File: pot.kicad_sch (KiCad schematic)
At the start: 7 parts, among them U24 LUM-1502-03_3.5mm_mono_vertic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, U3 LM324

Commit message: almost messed up the opamp :)
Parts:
- renumbered D30 to D1, R78 to R15, R79 to R16, R80 to R17, RV13 to RV1, U3 to U1, U24 to U8
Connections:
- net at RV1.1, U1.1: now also U1.2 (-); no longer U1.3 (+)
- net at R16.2, R17.1: now also U1.3 (+); no longer U1.2 (-)
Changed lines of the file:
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@@
   (symbol (lib_id "eurorack:LUM-1502-03_3.5mm_mono_vertical_jack") (at 33.655 67.31 0) (mirror x)
     (in_bom yes) (on_board yes) (fields_autoplaced)
-    (property "Reference" "U24" (id 0) (at 28.575 65.4049 0)
+    (property "Reference" "U8" (id 0) (at 28.575 65.4049 0)
       (effects (font (size 1.27 1.27)) (justify right))
     )
@@
     (pin "TN")
   )
-  (symbol (lib_id "eurorack:LM324") (at 88.265 63.5 0)
+  (symbol (lib_id "eurorack:LM324") (at 88.265 63.5 0) (mirror x)
     (in_bom yes) (on_board yes) (fields_autoplaced)
-    (property "Reference" "U3" (id 0) (at 88.265 53.34 0))
+    (property "Reference" "U1" (id 0) (at 88.265 53.34 0))
     (property "Value" "LM324" (id 1) (at 88.265 55.88 0))
-    (property "Footprint" "Package_SO:SO-14_3.9x8.65mm_P1.27mm" (id 2) (at 86.995 60.96 0)
+    (property "Footprint" "Package_SO:SO-14_3.9x8.65mm_P1.27mm" (id 2) (at 86.995 66.04 0)
       (effects (font (size 1.27 1.27)) hide)
     )
-    (property "Datasheet" "http://www.ti.com/lit/ds/symlink/lm2902-n.pdf" (id 3) (at 89.535 58.42 0)
+    (property "Datasheet" "http://www.ti.com/lit/ds/symlink/lm2902-n.pdf" (id 3) (at 89.535 68.58 0)
       (effects (font (size 1.27 1.27)) hide)
     )
-    (pin "12")
-    (pin "13")
-    (pin "14")
+    (pin "1")
+    (pin "2")
+    (pin "3")
   )
   (symbol (lib_id "power:GND") (at 39.37 71.12 0) (mirror y)
     (in_bom yes) (on_board yes) (fields_autoplaced)
-    (property "Reference" "#PWR0112" (id 0) (at 39.37 77.47 0)
+    (property "Reference" "#PWR033" (id 0) (at 39.37 77.47 0)
       (effects (font (size 1.27 1.27)) hide)
     )
@@
   (symbol (lib_id "eurorack:BAS 85 VIS") (at 47.625 66.04 180)
     (in_bom yes) (on_board yes) (fields_autoplaced)
-    (property "Reference" "D30" (id 0) (at 47.625 59.055 0))
+    (property "Reference" "D1" (id 0) (at 47.625 59.055 0))
     (property "Value" "BAS 85 VIS" (id 1) (at 47.625 61.595 0))
     (property "Footprint" "Diode_SMD:D_MiniMELF" (id 2) (at 47.625 61.595 0)
@@
   (symbol (lib_id "power:GND") (at 102.87 76.2 0)
     (in_bom yes) (on_board yes) (fields_autoplaced)
-    (property "Reference" "#PWR0114" (id 0) (at 102.87 82.55 0)
+    (property "Reference" "#PWR035" (id 0) (at 102.87 82.55 0)
       (effects (font (size 1.27 1.27)) hide)
     )
@@
   (symbol (lib_id "eurorack:Pot_500") (at 102.87 71.12 0)
     (in_bom yes) (on_board yes) (fields_autoplaced)
-    (property "Reference" "RV13" (id 0) (at 100.965 69.8499 0)
+    (property "Reference" "RV1" (id 0) (at 100.965 69.8499 0)
       (effects (font (size 1.27 1.27)) (justify right))
     )
@@
   (symbol (lib_id "eurorack:R-2k-0805") (at 68.58 69.85 0)
     (in_bom yes) (on_board yes) (fields_autoplaced)
-    (property "Reference" "R80" (id 0) (at 71.12 68.5799 0)
+    (property "Reference" "R17" (id 0) (at 71.12 68.5799 0)
       (effects (font (size 1.27 1.27)) (justify left))
     )
@@
   (symbol (lib_id "eurorack:R-2k-0805") (at 39.37 54.61 0)
     (in_bom yes) (on_board yes) (fields_autoplaced)
-    (property "Reference" "R78" (id 0) (at 41.91 53.3399 0)
+    (property "Reference" "R15" (id 0) (at 41.91 53.3399 0)
       (effects (font (size 1.27 1.27)) (justify left))
     )
@@
   (symbol (lib_id "power:+12V") (at 39.37 49.53 0)
     (in_bom yes) (on_board yes) (fields_autoplaced)
-    (property "Reference" "#PWR0111" (id 0) (at 39.37 53.34 0)
+    (property "Reference" "#PWR032" (id 0) (at 39.37 53.34 0)
       (effects (font (size 1.27 1.27)) hide)
     )
@@
   (symbol (lib_id "power:GND") (at 68.58 75.565 0)
     (in_bom yes) (on_board yes) (fields_autoplaced)
-    (property "Reference" "#PWR0113" (id 0) (at 68.58 81.915 0)
+    (property "Reference" "#PWR034" (id 0) (at 68.58 81.915 0)
       (effects (font (size 1.27 1.27)) hide)
     )
@@
   (symbol (lib_id "eurorack:R-7k5-0805") (at 60.325 66.04 90)
     (in_bom yes) (on_board yes) (fields_autoplaced)
-    (property "Reference" "R79" (id 0) (at 60.325 59.69 90))
+    (property "Reference" "R16" (id 0) (at 60.325 59.69 90))
     (property "Value" "R-7k5-0805" (id 1) (at 60.325 62.23 90))
     (property "Footprint" "Resistor_SMD:R_0805_2012Metric" (id 2) (at 60.325 67.818 90)

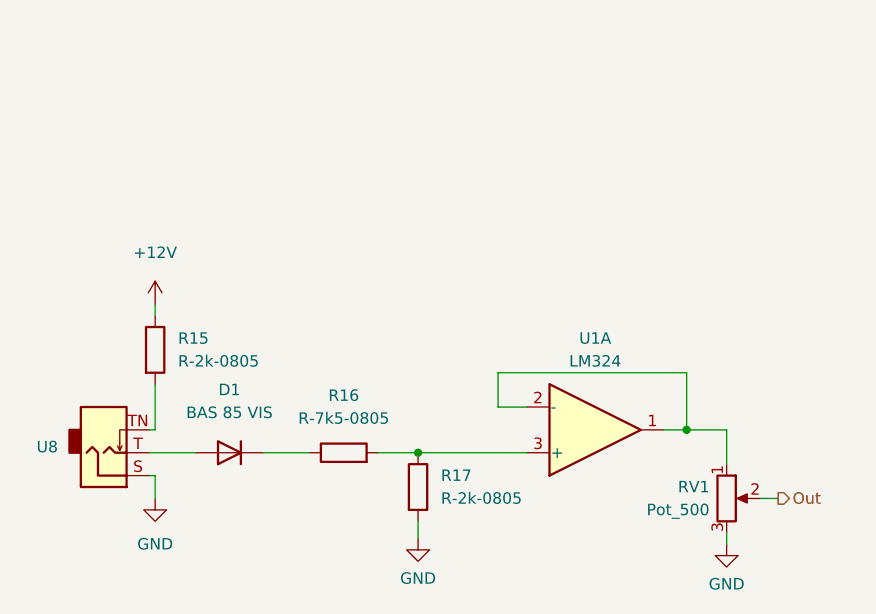
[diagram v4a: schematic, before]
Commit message: Made the first proposed layout
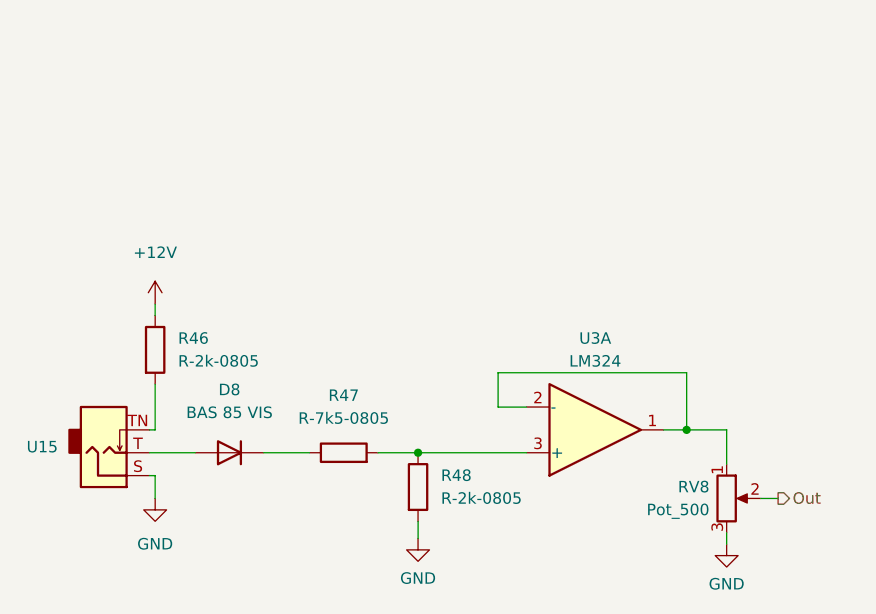
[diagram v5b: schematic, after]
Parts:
- renumbered D1 to D8, R15 to R46, R16 to R47, R17 to R48, RV1 to RV8, U8 to U15, U1 to U3
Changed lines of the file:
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@@
   (symbol (lib_id "eurorack:LUM-1502-03_3.5mm_mono_vertical_jack") (at 33.655 67.31 0) (mirror x)
     (in_bom yes) (on_board yes) (fields_autoplaced)
-    (property "Reference" "U8" (id 0) (at 28.575 65.4049 0)
+    (property "Reference" "U15" (id 0) (at 28.575 65.4049 0)
       (effects (font (size 1.27 1.27)) (justify right))
     )
@@
   (symbol (lib_id "eurorack:LM324") (at 88.265 63.5 0) (mirror x)
     (in_bom yes) (on_board yes) (fields_autoplaced)
-    (property "Reference" "U1" (id 0) (at 88.265 53.34 0))
+    (property "Reference" "U3" (id 0) (at 88.265 53.34 0))
     (property "Value" "LM324" (id 1) (at 88.265 55.88 0))
     (property "Footprint" "Package_SO:SO-14_3.9x8.65mm_P1.27mm" (id 2) (at 86.995 66.04 0)
@@
   (symbol (lib_id "power:GND") (at 39.37 71.12 0) (mirror y)
     (in_bom yes) (on_board yes) (fields_autoplaced)
-    (property "Reference" "#PWR033" (id 0) (at 39.37 77.47 0)
+    (property "Reference" "#PWR071" (id 0) (at 39.37 77.47 0)
       (effects (font (size 1.27 1.27)) hide)
     )
@@
   (symbol (lib_id "eurorack:BAS 85 VIS") (at 47.625 66.04 180)
     (in_bom yes) (on_board yes) (fields_autoplaced)
-    (property "Reference" "D1" (id 0) (at 47.625 59.055 0))
+    (property "Reference" "D8" (id 0) (at 47.625 59.055 0))
     (property "Value" "BAS 85 VIS" (id 1) (at 47.625 61.595 0))
     (property "Footprint" "Diode_SMD:D_MiniMELF" (id 2) (at 47.625 61.595 0)
@@
   (symbol (lib_id "power:GND") (at 102.87 76.2 0)
     (in_bom yes) (on_board yes) (fields_autoplaced)
-    (property "Reference" "#PWR035" (id 0) (at 102.87 82.55 0)
+    (property "Reference" "#PWR073" (id 0) (at 102.87 82.55 0)
       (effects (font (size 1.27 1.27)) hide)
     )
@@
   (symbol (lib_id "eurorack:Pot_500") (at 102.87 71.12 0)
     (in_bom yes) (on_board yes) (fields_autoplaced)
-    (property "Reference" "RV1" (id 0) (at 100.965 69.8499 0)
+    (property "Reference" "RV8" (id 0) (at 100.965 69.8499 0)
       (effects (font (size 1.27 1.27)) (justify right))
     )
@@
   (symbol (lib_id "eurorack:R-2k-0805") (at 68.58 69.85 0)
     (in_bom yes) (on_board yes) (fields_autoplaced)
-    (property "Reference" "R17" (id 0) (at 71.12 68.5799 0)
+    (property "Reference" "R48" (id 0) (at 71.12 68.5799 0)
       (effects (font (size 1.27 1.27)) (justify left))
     )
@@
   (symbol (lib_id "eurorack:R-2k-0805") (at 39.37 54.61 0)
     (in_bom yes) (on_board yes) (fields_autoplaced)
-    (property "Reference" "R15" (id 0) (at 41.91 53.3399 0)
+    (property "Reference" "R46" (id 0) (at 41.91 53.3399 0)
       (effects (font (size 1.27 1.27)) (justify left))
     )
@@
   (symbol (lib_id "power:+12V") (at 39.37 49.53 0)
     (in_bom yes) (on_board yes) (fields_autoplaced)
-    (property "Reference" "#PWR032" (id 0) (at 39.37 53.34 0)
+    (property "Reference" "#PWR070" (id 0) (at 39.37 53.34 0)
       (effects (font (size 1.27 1.27)) hide)
     )
@@
   (symbol (lib_id "power:GND") (at 68.58 75.565 0)
     (in_bom yes) (on_board yes) (fields_autoplaced)
-    (property "Reference" "#PWR034" (id 0) (at 68.58 81.915 0)
+    (property "Reference" "#PWR072" (id 0) (at 68.58 81.915 0)
       (effects (font (size 1.27 1.27)) hide)
     )
@@
   (symbol (lib_id "eurorack:R-7k5-0805") (at 60.325 66.04 90)
     (in_bom yes) (on_board yes) (fields_autoplaced)
-    (property "Reference" "R16" (id 0) (at 60.325 59.69 90))
+    (property "Reference" "R47" (id 0) (at 60.325 59.69 90))
     (property "Value" "R-7k5-0805" (id 1) (at 60.325 62.23 90))
     (property "Footprint" "Resistor_SMD:R_0805_2012Metric" (id 2) (at 60.325 67.818 90)

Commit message: working on the PCB
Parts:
- renumbered D8 to D1, R46 to R15, R47 to R16, R48 to R17, RV8 to RV1, U3 to U1, U15 to U8
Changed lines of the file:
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@@
   (symbol (lib_id "eurorack:LUM-1502-03_3.5mm_mono_vertical_jack") (at 33.655 67.31 0) (mirror x)
     (in_bom yes) (on_board yes) (fields_autoplaced)
-    (property "Reference" "U15" (id 0) (at 28.575 65.4049 0)
+    (property "Reference" "U8" (id 0) (at 28.575 65.4049 0)
       (effects (font (size 1.27 1.27)) (justify right))
     )
@@
   (symbol (lib_id "eurorack:LM324") (at 88.265 63.5 0) (mirror x)
     (in_bom yes) (on_board yes) (fields_autoplaced)
-    (property "Reference" "U3" (id 0) (at 88.265 53.34 0))
+    (property "Reference" "U1" (id 0) (at 88.265 53.34 0))
     (property "Value" "LM324" (id 1) (at 88.265 55.88 0))
     (property "Footprint" "Package_SO:SO-14_3.9x8.65mm_P1.27mm" (id 2) (at 86.995 66.04 0)
@@
   (symbol (lib_id "power:GND") (at 39.37 71.12 0) (mirror y)
     (in_bom yes) (on_board yes) (fields_autoplaced)
-    (property "Reference" "#PWR071" (id 0) (at 39.37 77.47 0)
+    (property "Reference" "#PWR0112" (id 0) (at 39.37 77.47 0)
       (effects (font (size 1.27 1.27)) hide)
     )
@@
   (symbol (lib_id "eurorack:BAS 85 VIS") (at 47.625 66.04 180)
     (in_bom yes) (on_board yes) (fields_autoplaced)
-    (property "Reference" "D8" (id 0) (at 47.625 59.055 0))
+    (property "Reference" "D1" (id 0) (at 47.625 59.055 0))
     (property "Value" "BAS 85 VIS" (id 1) (at 47.625 61.595 0))
     (property "Footprint" "Diode_SMD:D_MiniMELF" (id 2) (at 47.625 61.595 0)
@@
   (symbol (lib_id "power:GND") (at 102.87 76.2 0)
     (in_bom yes) (on_board yes) (fields_autoplaced)
-    (property "Reference" "#PWR073" (id 0) (at 102.87 82.55 0)
+    (property "Reference" "#PWR0114" (id 0) (at 102.87 82.55 0)
       (effects (font (size 1.27 1.27)) hide)
     )
@@
   (symbol (lib_id "eurorack:Pot_500") (at 102.87 71.12 0)
     (in_bom yes) (on_board yes) (fields_autoplaced)
-    (property "Reference" "RV8" (id 0) (at 100.965 69.8499 0)
+    (property "Reference" "RV1" (id 0) (at 100.965 69.8499 0)
       (effects (font (size 1.27 1.27)) (justify right))
     )
@@
   (symbol (lib_id "eurorack:R-2k-0805") (at 68.58 69.85 0)
     (in_bom yes) (on_board yes) (fields_autoplaced)
-    (property "Reference" "R48" (id 0) (at 71.12 68.5799 0)
+    (property "Reference" "R17" (id 0) (at 71.12 68.5799 0)
       (effects (font (size 1.27 1.27)) (justify left))
     )
@@
   (symbol (lib_id "eurorack:R-2k-0805") (at 39.37 54.61 0)
     (in_bom yes) (on_board yes) (fields_autoplaced)
-    (property "Reference" "R46" (id 0) (at 41.91 53.3399 0)
+    (property "Reference" "R15" (id 0) (at 41.91 53.3399 0)
       (effects (font (size 1.27 1.27)) (justify left))
     )
@@
   (symbol (lib_id "power:+12V") (at 39.37 49.53 0)
     (in_bom yes) (on_board yes) (fields_autoplaced)
-    (property "Reference" "#PWR070" (id 0) (at 39.37 53.34 0)
+    (property "Reference" "#PWR0111" (id 0) (at 39.37 53.34 0)
       (effects (font (size 1.27 1.27)) hide)
     )
@@
   (symbol (lib_id "power:GND") (at 68.58 75.565 0)
     (in_bom yes) (on_board yes) (fields_autoplaced)
-    (property "Reference" "#PWR072" (id 0) (at 68.58 81.915 0)
+    (property "Reference" "#PWR0113" (id 0) (at 68.58 81.915 0)
       (effects (font (size 1.27 1.27)) hide)
     )
@@
   (symbol (lib_id "eurorack:R-7k5-0805") (at 60.325 66.04 90)
     (in_bom yes) (on_board yes) (fields_autoplaced)
-    (property "Reference" "R47" (id 0) (at 60.325 59.69 90))
+    (property "Reference" "R16" (id 0) (at 60.325 59.69 90))
     (property "Value" "R-7k5-0805" (id 1) (at 60.325 62.23 90))
     (property "Footprint" "Resistor_SMD:R_0805_2012Metric" (id 2) (at 60.325 67.818 90)

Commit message: working on PCB
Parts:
- renumbered D1 to D28, R15 to R72, R16 to R73, R17 to R74, RV1 to RV11, U8 to U22, U1 to U3
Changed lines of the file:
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@@
   (symbol (lib_id "eurorack:LUM-1502-03_3.5mm_mono_vertical_jack") (at 33.655 67.31 0) (mirror x)
     (in_bom yes) (on_board yes) (fields_autoplaced)
-    (property "Reference" "U8" (id 0) (at 28.575 65.4049 0)
+    (property "Reference" "U22" (id 0) (at 28.575 65.4049 0)
       (effects (font (size 1.27 1.27)) (justify right))
     )
@@
   (symbol (lib_id "eurorack:LM324") (at 88.265 63.5 0) (mirror x)
     (in_bom yes) (on_board yes) (fields_autoplaced)
-    (property "Reference" "U1" (id 0) (at 88.265 53.34 0))
+    (property "Reference" "U3" (id 0) (at 88.265 53.34 0))
     (property "Value" "LM324" (id 1) (at 88.265 55.88 0))
     (property "Footprint" "Package_SO:SO-14_3.9x8.65mm_P1.27mm" (id 2) (at 86.995 66.04 0)
@@
       (effects (font (size 1.27 1.27)) hide)
     )
-    (pin "1")
-    (pin "2")
-    (pin "3")
+    (pin "5")
+    (pin "6")
+    (pin "7")
   )
   (symbol (lib_id "power:GND") (at 39.37 71.12 0) (mirror y)
     (in_bom yes) (on_board yes) (fields_autoplaced)
-    (property "Reference" "#PWR0112" (id 0) (at 39.37 77.47 0)
+    (property "Reference" "#PWR0104" (id 0) (at 39.37 77.47 0)
       (effects (font (size 1.27 1.27)) hide)
     )
@@
   (symbol (lib_id "eurorack:BAS 85 VIS") (at 47.625 66.04 180)
     (in_bom yes) (on_board yes) (fields_autoplaced)
-    (property "Reference" "D1" (id 0) (at 47.625 59.055 0))
+    (property "Reference" "D28" (id 0) (at 47.625 59.055 0))
     (property "Value" "BAS 85 VIS" (id 1) (at 47.625 61.595 0))
     (property "Footprint" "Diode_SMD:D_MiniMELF" (id 2) (at 47.625 61.595 0)
@@
   (symbol (lib_id "power:GND") (at 102.87 76.2 0)
     (in_bom yes) (on_board yes) (fields_autoplaced)
-    (property "Reference" "#PWR0114" (id 0) (at 102.87 82.55 0)
+    (property "Reference" "#PWR0106" (id 0) (at 102.87 82.55 0)
       (effects (font (size 1.27 1.27)) hide)
     )
@@
   (symbol (lib_id "eurorack:Pot_500") (at 102.87 71.12 0)
     (in_bom yes) (on_board yes) (fields_autoplaced)
-    (property "Reference" "RV1" (id 0) (at 100.965 69.8499 0)
+    (property "Reference" "RV11" (id 0) (at 100.33 69.8499 0)
       (effects (font (size 1.27 1.27)) (justify right))
     )
-    (property "Value" "Pot_500" (id 1) (at 100.965 72.3899 0)
+    (property "Value" "Pot_500" (id 1) (at 100.33 72.3899 0)
       (effects (font (size 1.27 1.27)) (justify right))
     )
@@
   (symbol (lib_id "eurorack:R-2k-0805") (at 68.58 69.85 0)
     (in_bom yes) (on_board yes) (fields_autoplaced)
-    (property "Reference" "R17" (id 0) (at 71.12 68.5799 0)
+    (property "Reference" "R74" (id 0) (at 71.12 68.5799 0)
       (effects (font (size 1.27 1.27)) (justify left))
     )
@@
   (symbol (lib_id "eurorack:R-2k-0805") (at 39.37 54.61 0)
     (in_bom yes) (on_board yes) (fields_autoplaced)
-    (property "Reference" "R15" (id 0) (at 41.91 53.3399 0)
+    (property "Reference" "R72" (id 0) (at 41.91 53.3399 0)
       (effects (font (size 1.27 1.27)) (justify left))
     )
@@
   (symbol (lib_id "power:+12V") (at 39.37 49.53 0)
     (in_bom yes) (on_board yes) (fields_autoplaced)
-    (property "Reference" "#PWR0111" (id 0) (at 39.37 53.34 0)
+    (property "Reference" "#PWR0103" (id 0) (at 39.37 53.34 0)
       (effects (font (size 1.27 1.27)) hide)
     )
@@
   (symbol (lib_id "power:GND") (at 68.58 75.565 0)
     (in_bom yes) (on_board yes) (fields_autoplaced)
-    (property "Reference" "#PWR0113" (id 0) (at 68.58 81.915 0)
+    (property "Reference" "#PWR0105" (id 0) (at 68.58 81.915 0)
       (effects (font (size 1.27 1.27)) hide)
     )
@@
   (symbol (lib_id "eurorack:R-7k5-0805") (at 60.325 66.04 90)
     (in_bom yes) (on_board yes) (fields_autoplaced)
-    (property "Reference" "R16" (id 0) (at 60.325 59.69 90))
+    (property "Reference" "R73" (id 0) (at 60.325 59.69 90))
     (property "Value" "R-7k5-0805" (id 1) (at 60.325 62.23 90))
     (property "Footprint" "Resistor_SMD:R_0805_2012Metric" (id 2) (at 60.325 67.818 90)

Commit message: working on PCB, new iteratrion
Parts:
- renumbered D28 to D5, R72 to R27, R73 to R28, R74 to R29, RV11 to RV5, U22 to U12, U3 to U2
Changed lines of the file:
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@@
   (symbol (lib_id "eurorack:LUM-1502-03_3.5mm_mono_vertical_jack") (at 33.655 67.31 0) (mirror x)
     (in_bom yes) (on_board yes) (fields_autoplaced)
-    (property "Reference" "U22" (id 0) (at 28.575 65.4049 0)
+    (property "Reference" "U12" (id 0) (at 28.575 65.4049 0)
       (effects (font (size 1.27 1.27)) (justify right))
     )
@@
   (symbol (lib_id "eurorack:LM324") (at 88.265 63.5 0) (mirror x)
     (in_bom yes) (on_board yes) (fields_autoplaced)
-    (property "Reference" "U3" (id 0) (at 88.265 53.34 0))
+    (property "Reference" "U2" (id 0) (at 88.265 53.34 0))
     (property "Value" "LM324" (id 1) (at 88.265 55.88 0))
     (property "Footprint" "Package_SO:SO-14_3.9x8.65mm_P1.27mm" (id 2) (at 86.995 66.04 0)
@@
       (effects (font (size 1.27 1.27)) hide)
     )
-    (pin "5")
-    (pin "6")
-    (pin "7")
+    (pin "1")
+    (pin "2")
+    (pin "3")
   )
   (symbol (lib_id "power:GND") (at 39.37 71.12 0) (mirror y)
     (in_bom yes) (on_board yes) (fields_autoplaced)
-    (property "Reference" "#PWR0104" (id 0) (at 39.37 77.47 0)
+    (property "Reference" "#PWR0112" (id 0) (at 39.37 77.47 0)
       (effects (font (size 1.27 1.27)) hide)
     )
@@
   (symbol (lib_id "eurorack:BAS 85 VIS") (at 47.625 66.04 180)
     (in_bom yes) (on_board yes) (fields_autoplaced)
-    (property "Reference" "D28" (id 0) (at 47.625 59.055 0))
+    (property "Reference" "D5" (id 0) (at 47.625 59.055 0))
     (property "Value" "BAS 85 VIS" (id 1) (at 47.625 61.595 0))
     (property "Footprint" "Diode_SMD:D_MiniMELF" (id 2) (at 47.625 61.595 0)
@@
   (symbol (lib_id "power:GND") (at 102.87 76.2 0)
     (in_bom yes) (on_board yes) (fields_autoplaced)
-    (property "Reference" "#PWR0106" (id 0) (at 102.87 82.55 0)
+    (property "Reference" "#PWR0114" (id 0) (at 102.87 82.55 0)
       (effects (font (size 1.27 1.27)) hide)
     )
@@
   (symbol (lib_id "eurorack:Pot_500") (at 102.87 71.12 0)
     (in_bom yes) (on_board yes) (fields_autoplaced)
-    (property "Reference" "RV11" (id 0) (at 100.33 69.8499 0)
+    (property "Reference" "RV5" (id 0) (at 100.33 69.8499 0)
       (effects (font (size 1.27 1.27)) (justify right))
     )
@@
   (symbol (lib_id "eurorack:R-2k-0805") (at 68.58 69.85 0)
     (in_bom yes) (on_board yes) (fields_autoplaced)
-    (property "Reference" "R74" (id 0) (at 71.12 68.5799 0)
+    (property "Reference" "R29" (id 0) (at 71.12 68.5799 0)
       (effects (font (size 1.27 1.27)) (justify left))
     )
@@
   (symbol (lib_id "eurorack:R-2k-0805") (at 39.37 54.61 0)
     (in_bom yes) (on_board yes) (fields_autoplaced)
-    (property "Reference" "R72" (id 0) (at 41.91 53.3399 0)
+    (property "Reference" "R27" (id 0) (at 41.91 53.3399 0)
       (effects (font (size 1.27 1.27)) (justify left))
     )
@@
   (symbol (lib_id "power:+12V") (at 39.37 49.53 0)
     (in_bom yes) (on_board yes) (fields_autoplaced)
-    (property "Reference" "#PWR0103" (id 0) (at 39.37 53.34 0)
+    (property "Reference" "#PWR0111" (id 0) (at 39.37 53.34 0)
       (effects (font (size 1.27 1.27)) hide)
     )
@@
   (symbol (lib_id "power:GND") (at 68.58 75.565 0)
     (in_bom yes) (on_board yes) (fields_autoplaced)
-    (property "Reference" "#PWR0105" (id 0) (at 68.58 81.915 0)
+    (property "Reference" "#PWR0113" (id 0) (at 68.58 81.915 0)
       (effects (font (size 1.27 1.27)) hide)
     )
@@
   (symbol (lib_id "eurorack:R-7k5-0805") (at 60.325 66.04 90)
     (in_bom yes) (on_board yes) (fields_autoplaced)
-    (property "Reference" "R73" (id 0) (at 60.325 59.69 90))
+    (property "Reference" "R28" (id 0) (at 60.325 59.69 90))
     (property "Value" "R-7k5-0805" (id 1) (at 60.325 62.23 90))
     (property "Footprint" "Resistor_SMD:R_0805_2012Metric" (id 2) (at 60.325 67.818 90)
